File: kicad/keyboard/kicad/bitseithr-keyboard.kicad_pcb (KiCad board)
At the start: 4 copper layers, 365 x 206 mm, 105 parts, among them P2 KEYB CONN 1

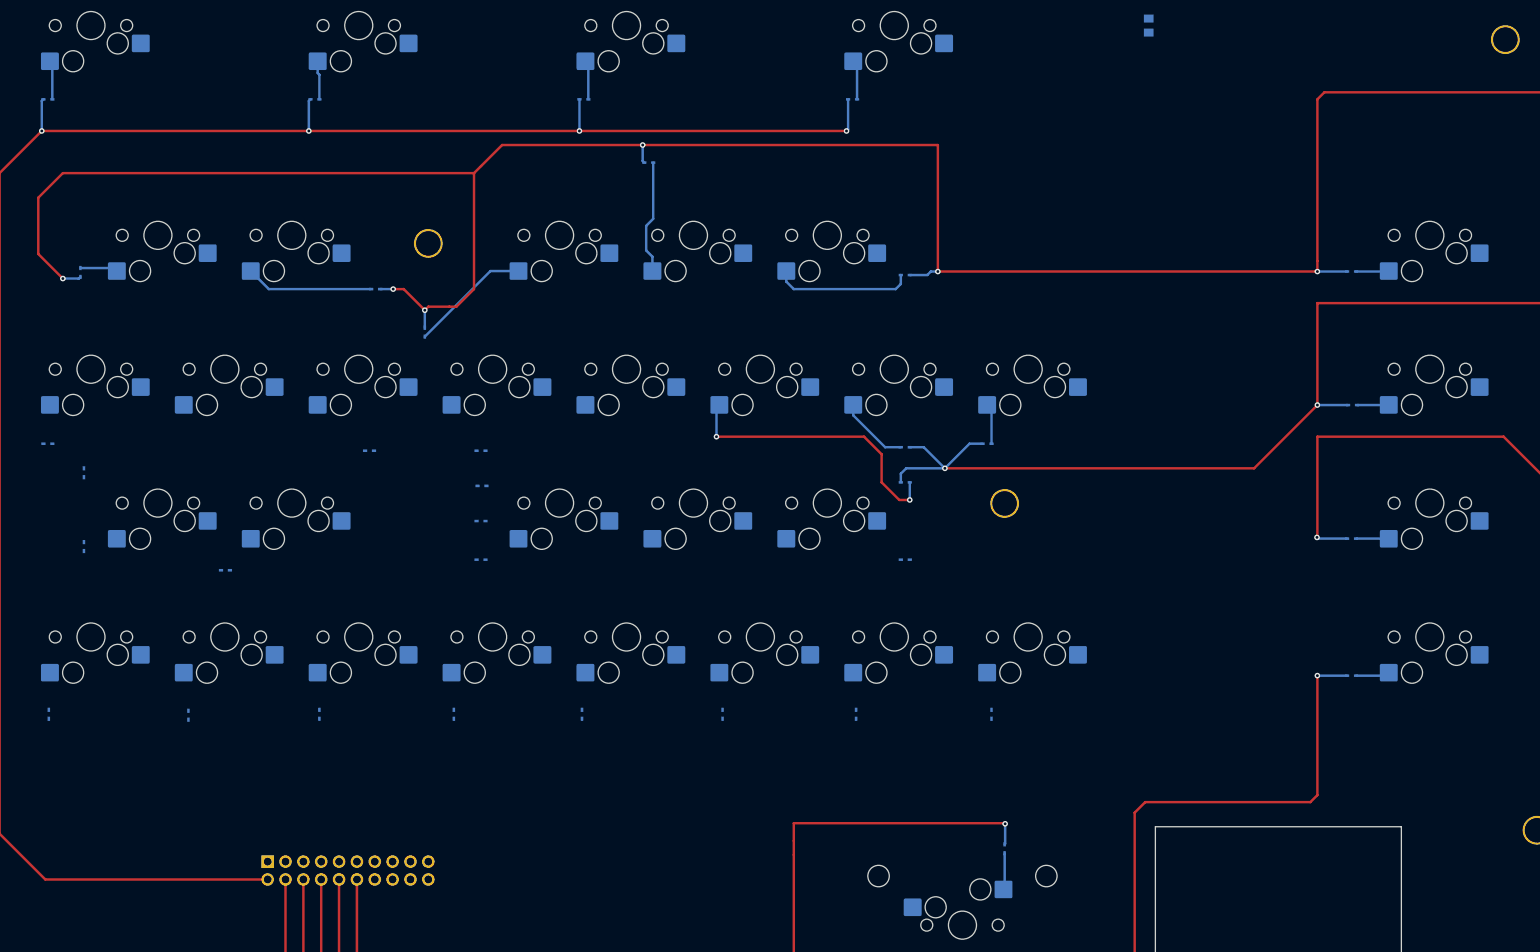
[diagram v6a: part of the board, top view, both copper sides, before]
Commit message: updated keyboard connector pinout again for better routing
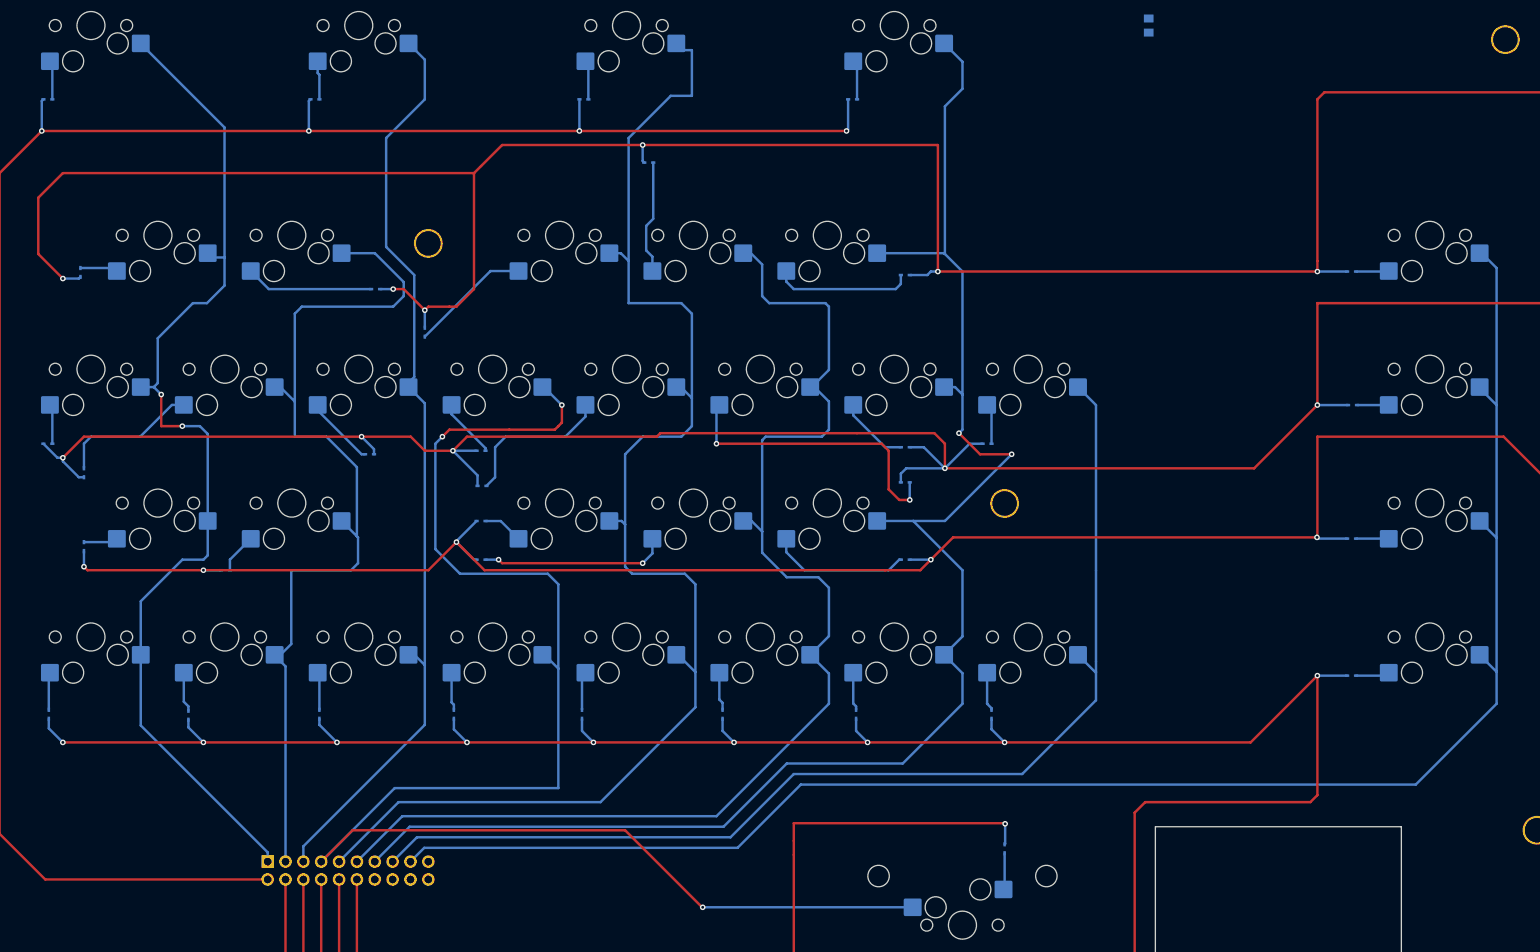
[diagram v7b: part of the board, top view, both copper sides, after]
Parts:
- moved D12 0.50 mm to (101.6, 159.0), turned to 180 degrees
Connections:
- MX1 pad 1: unconnected-(MX1-COL-Pad1) -> COL0
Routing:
- net COL8: track 0.00 -> 239.5 mm
- net COL6: track 0.00 -> 227.4 mm, vias 0 -> 2
- net COL3: track 0.00 -> 220.9 mm, vias 0 -> 3
- net ROW4: track 212.1 -> 427.6 mm, vias 1 -> 9
- net COL4: track 0.00 -> 197.5 mm
- net ROW3: track 333.2 -> 529.9 mm, vias 1 -> 5
- net COL5: track 0.00 -> 174.4 mm
- net COL7: track 0.00 -> 158.8 mm
- net ROW2: track 442.8 -> 596.6 mm, vias 2 -> 5
- net COL0: track 0.00 -> 150.8 mm, vias 0 -> 2
- net COL2: track 0.00 -> 132.7 mm
- net COL1: track 0.00 -> 131.2 mm
- net Net-(D24-A): track 0.00 -> 26.6 mm, vias 0 -> 2
- net Net-(D19-A): track 0.00 -> 22.3 mm
- net Net-(D8-A): track 0.00 -> 20.0 mm
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
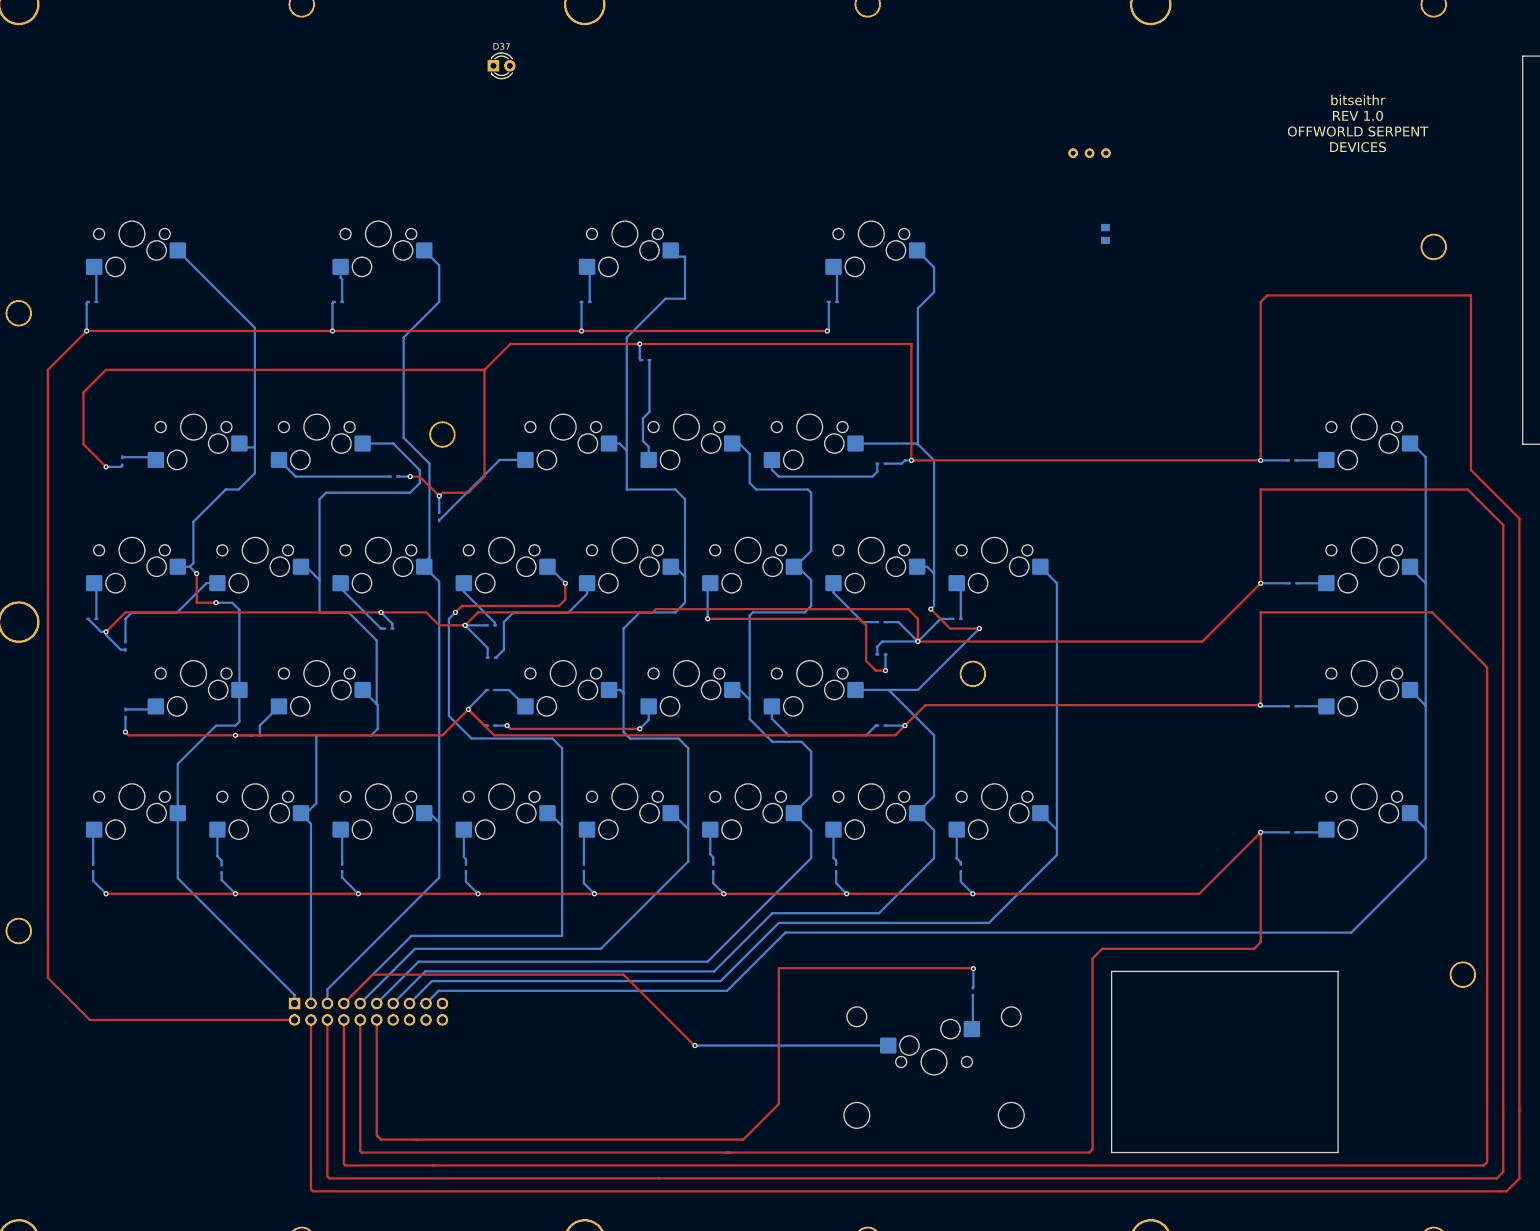
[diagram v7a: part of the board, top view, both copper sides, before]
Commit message: keyboard pcb ~mostly done (still need to ground the mounting holes)
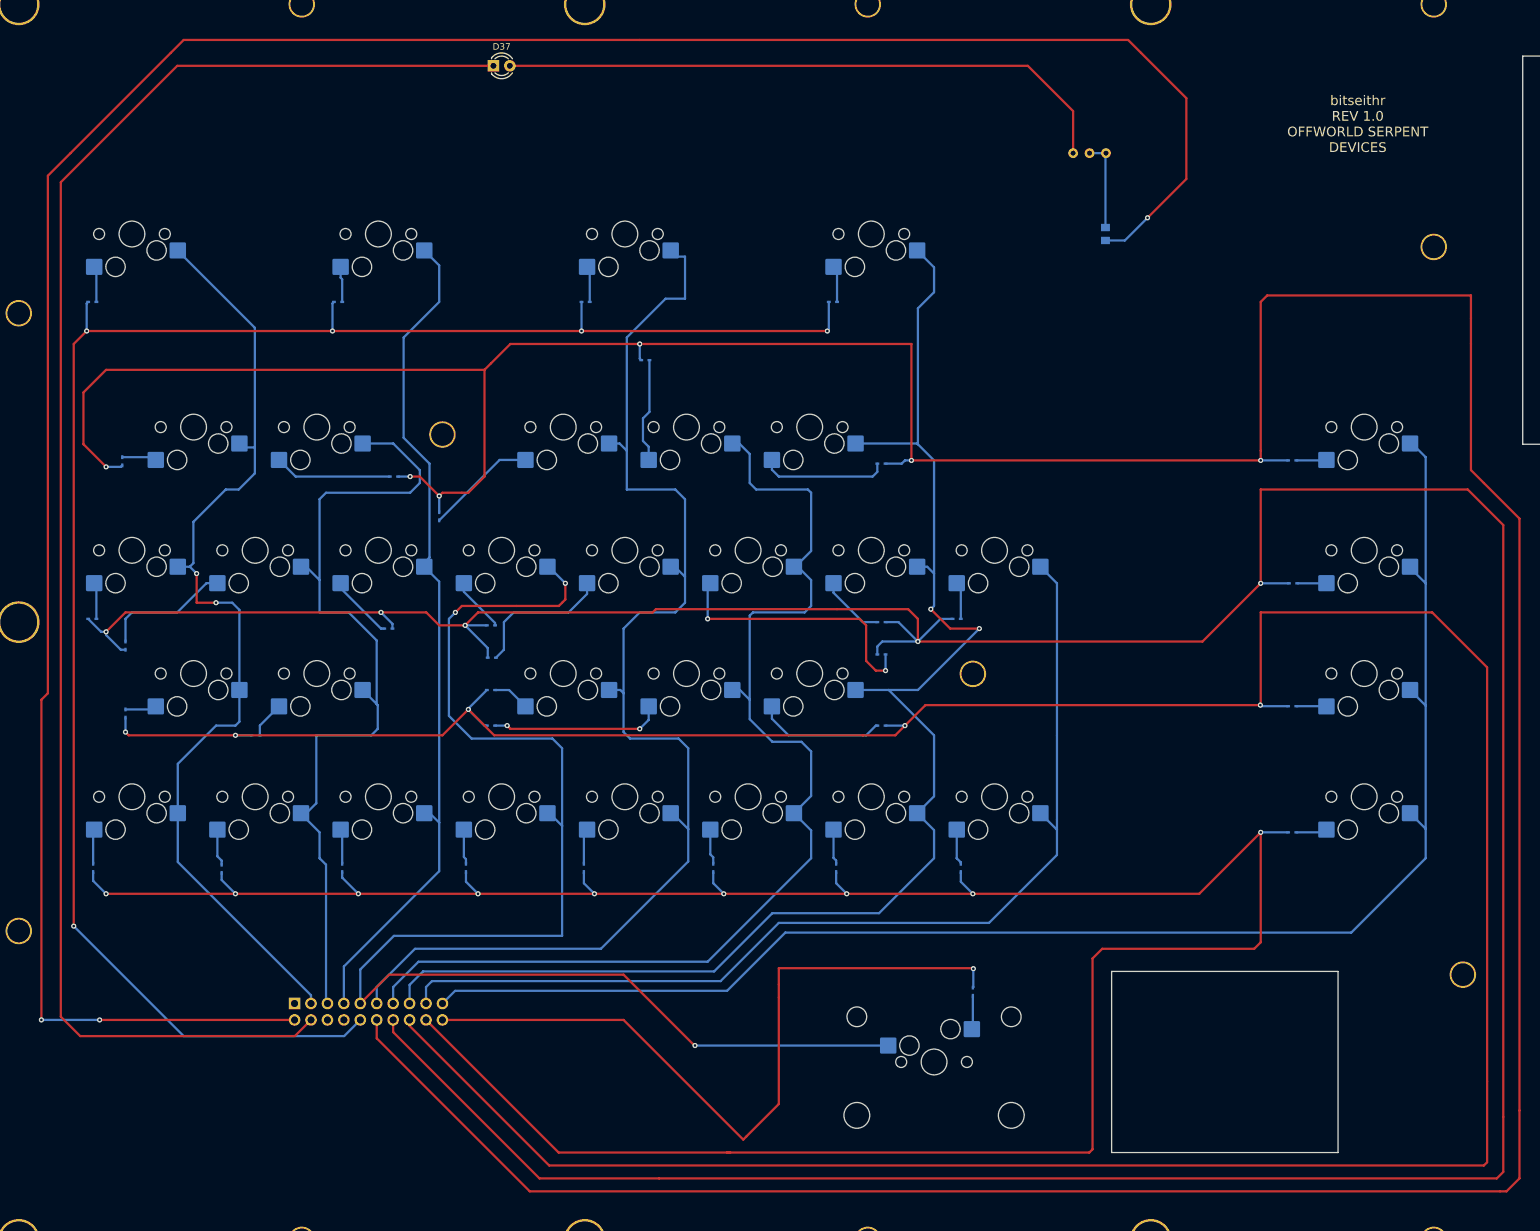
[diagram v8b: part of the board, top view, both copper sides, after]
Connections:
- P2 pad 1: COL0 -> unconnected-(P2-Pad1)
- P2 pad 10: ROW4 -> ROW0
- P2 pad 11: COL5 -> COL4
- P2 pad 12: ROW5 -> ROW1
- P2 pad 13: COL6 -> COL5
- P2 pad 14: unconnected-(P2-Pad14) -> ROW2
- P2 pad 15: COL7 -> COL6
- P2 pad 16: unconnected-(P2-Pad16) -> ROW3
- P2 pad 17: COL8 -> COL7
- P2 pad 18: GND -> ROW4
- P2 pad 19: unconnected-(P2-Pad19) -> COL8
- P2 pad 2: ROW0 -> +9V
- P2 pad 20: +9V -> ROW5
- P2 pad 3: COL1 -> COL0
- P2 pad 4: ROW1 -> GND
- P2 pad 5: COL2 -> COL1
- P2 pad 6: ROW2 -> unconnected-(P2-Pad6)
- P2 pad 7: COL3 -> COL2
- P2 pad 8: ROW3 -> unconnected-(P2-Pad8)
- P2 pad 9: COL4 -> COL3
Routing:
- net +9V: track 0.00 -> 387.4 mm, vias 0 -> 3
- net GND: track 0.00 -> 244.3 mm
- net Net-(D37-A): track 0.00 -> 96.5 mm
- net ROW1: track 675.5 -> 651.7 mm
- net ROW2: track 596.6 -> 573.3 mm
- net ROW3: track 529.9 -> 507.2 mm
- net ROW4: track 427.6 -> 405.5 mm
- net ROW5: track 136.5 -> 115.9 mm
- net Net-(R15-Pad1): track 0.00 -> 14.1 mm
- net COL8: track 239.5 -> 237.0 mm
- net COL3: track 220.9 -> 218.9 mm
- net ROW0: track 276.1 -> 278.0 mm, vias 4 -> 5
- net COL4: track 197.5 -> 196.4 mm
- net COL2: track 132.7 -> 131.6 mm
- net COL7: track 158.8 -> 157.7 mm
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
